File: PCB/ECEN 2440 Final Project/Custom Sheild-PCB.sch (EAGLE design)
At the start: 10 parts

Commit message: prettyfy schematic. vague shield board layout.
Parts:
- removed JP1: (no value), pinhead:PINHD-1X6
- added C1, C2, C3: 500n, rcl:C-USC0805
- added OI_1, OI_2, OI_3: (no value), pinhead:PINHD-1X3
- added R3, R4, R5: 100R, rcl:R-US_R0805
- added U$4: DRA_BREAKOUT, Custom Library:DRA_BREAKOUT
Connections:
- net CD1 renamed SD_CD1
- new net AUDIO_FILTERED: C3.1, R5.2, U$4.MIC_IN
- new net N$3: C1.1, R3.2, R4.1
- new net N$4: C2.1, R4.2, R5.1
- new net OI_1: OI_1.2, U$3.73
- new net OI_2: OI_2.2, U$3.70
- new net OI_3: OI_3.2, U$3.67
- new net PD_RADIO: U$4.PD
- new net RADIO_PD: U$3.35
- net +3V3: now also OI_1.3, OI_2.3, OI_3.3; no longer JP1.6
- net AUDIO_PTT: now also U$4.PTT; no longer JP1.4
- net AUDIO_PWM: now also R3.1; no longer JP1.3
- net GND: now also C1.2, C2.2, C3.2, OI_1.1, OI_2.1, OI_3.1, U$4.GND; no longer JP1.5
- net RX_RADIO: now also U$4.RX_RADIO; no longer JP1.2
- net TX_RADIO: now also U$4.TX_RADIO; no longer JP1.1
- net VCC: now also U$4.VBATT
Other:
- note added: "Altimeter and i2c"
- note added: "SD card options"
- note removed: "Radio Breakout Board Pin Hook Up"
- moved on the sheet: BATTERY, R1, R2, SD_BREAKOUT, SJ1, TEENSY, U$2

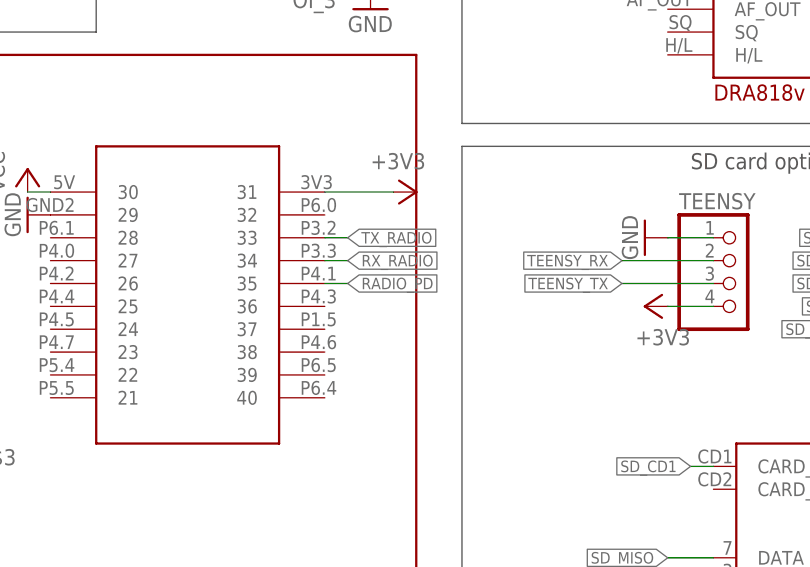
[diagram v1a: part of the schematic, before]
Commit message: changes to the traces of the shield board
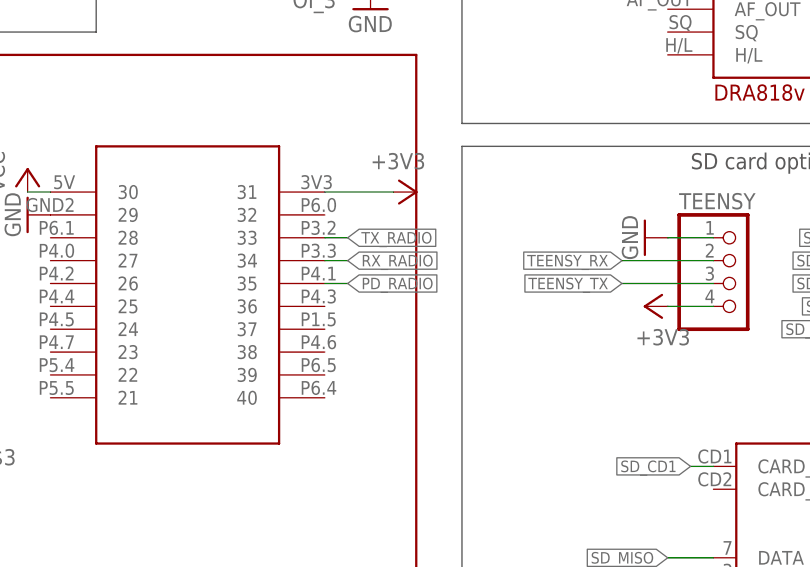
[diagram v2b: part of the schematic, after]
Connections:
- removed net RADIO_PD: U$3.35
- net PD_RADIO: now also U$3.35
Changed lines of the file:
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@@
 <?xml version="1.0" encoding="utf-8"?>
 <!DOCTYPE eagle SYSTEM "eagle.dtd">
-<eagle version="9.5.1">
+<eagle version="9.2.2">
 <drawing>
 <settings>
@@
 <label x="116.84" y="73.66" size="1.27" layer="95" rot="R180" xref="yes"/>
 </segment>
-</net>
-<net name="RADIO_PD" class="0">
 <segment>
 <pinref part="U$3" gate="MSP432" pin="35"/>

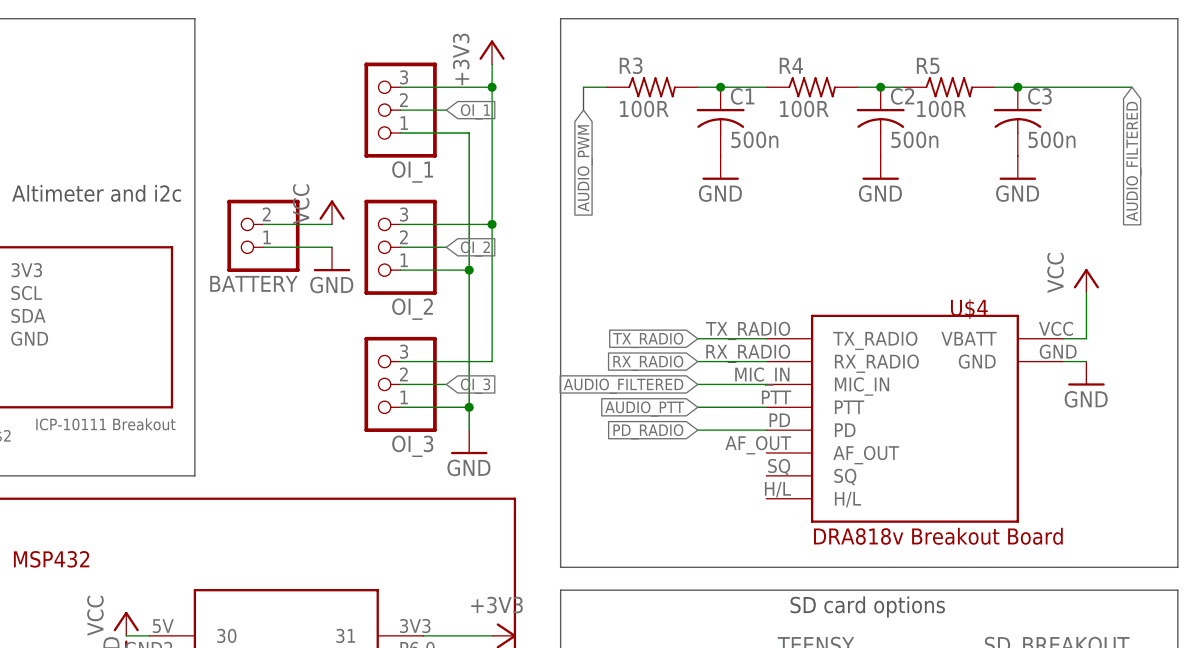
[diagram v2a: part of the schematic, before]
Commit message: changes to the traces of the sheild board
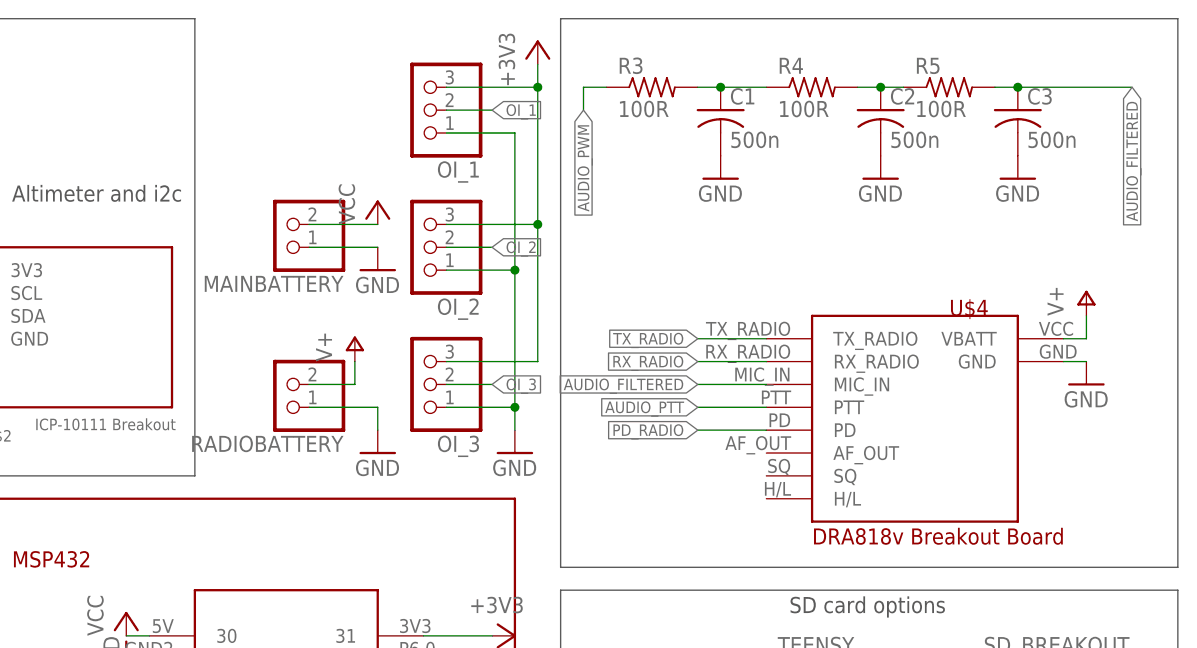
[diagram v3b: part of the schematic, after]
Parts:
- removed BATTERY: (no value), pinhead:PINHD-1X2
- added MAINBATTERY, RADIOBATTERY: (no value), pinhead:PINHD-1X2
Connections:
- new net V+: RADIOBATTERY.2, U$4.VBATT
- net GND: now also MAINBATTERY.1, RADIOBATTERY.1; no longer BATTERY.1
- net VCC: now also MAINBATTERY.2; no longer BATTERY.2, U$4.VBATT
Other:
- moved on the sheet: OI_1, OI_2, OI_3

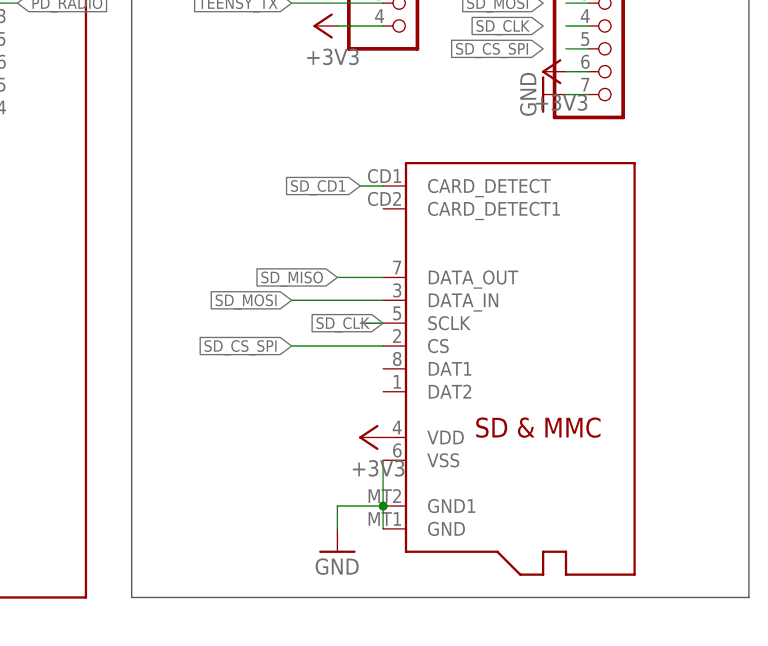
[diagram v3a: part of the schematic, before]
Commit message: changes to traces on sheild board
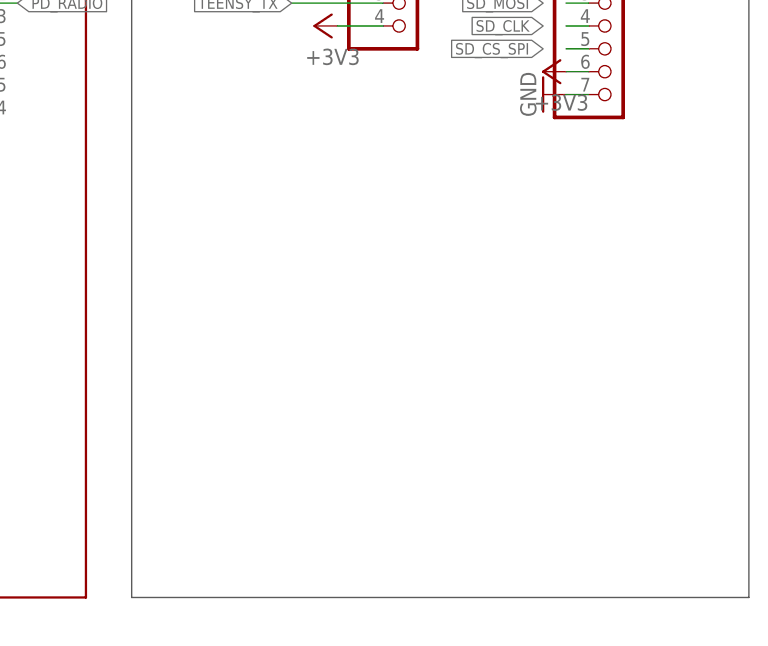
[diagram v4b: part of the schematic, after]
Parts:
- removed U$1: MICROSD, adafruit:MICROSD
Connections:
- net +3V3: no longer U$1.VDD
- net GND: no longer U$1.GND, U$1.GND1, U$1.VSS
- net SD_CD1: no longer U$1.CARD_DETECT
- net SD_CLK: no longer U$1.SCLK
- net SD_CS_SPI: no longer U$1.CS
- net SD_MISO: no longer U$1.DATA_OUT
- net SD_MOSI: no longer U$1.DATA_IN
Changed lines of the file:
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@@
 </classes>
 <parts>
-<part name="U$1" library="adafruit" library_urn="urn:adsk.eagle:library:420" deviceset="MICROSD" device="" package3d_urn="urn:adsk.eagle:package:6240723/1"/>
 <part name="U$2" library="Custom Library" deviceset="ALTIMETER" device=""/>
 <part name="U$3" library="Custom Library" deviceset="MSP432" device=""/>
 <part name="GND1" library="supply1" library_urn="urn:adsk.eagle:library:371" deviceset="GND" device=""/>
-<part name="GND2" library="supply1" library_urn="urn:adsk.eagle:library:371" deviceset="GND" device=""/>
 <part name="GND4" library="supply1" library_urn="urn:adsk.eagle:library:371" deviceset="GND" device=""/>
 <part name="GND5" library="supply1" library_urn="urn:adsk.eagle:library:371" deviceset="GND" device=""/>
 <part name="+3V1" library="supply1" library_urn="urn:adsk.eagle:library:371" deviceset="+3V3" device=""/>
 <part name="+3V2" library="supply1" library_urn="urn:adsk.eagle:library:371" deviceset="+3V3" device=""/>
-<part name="+3V3" library="supply1" library_urn="urn:adsk.eagle:library:371" deviceset="+3V3" device=""/>
 <part name="+3V5" library="supply1" library_urn="urn:adsk.eagle:library:371" deviceset="+3V3" device=""/>
 <part name="GND9" library="supply1" library_urn="urn:adsk.eagle:library:371" deviceset="GND" device=""/>
@@
 </plain>
 <instances>
-<instance part="U$1" gate="G$1" x="147.32" y="2.54" smashed="yes"/>
 <instance part="U$2" gate="G$1" x="38.1" y="76.2" smashed="yes">
 <attribute name="NAME" x="40.64" y="73.66" size="1.27" layer="95" rot="R180"/>
@@
 <attribute name="VALUE" x="25.4" y="76.2" size="1.778" layer="96"/>
 </instance>
-<instance part="GND2" gate="1" x="124.46" y="-20.32" smashed="yes">
-<attribute name="VALUE" x="121.92" y="-22.86" size="1.778" layer="96"/>
-</instance>
 <instance part="GND4" gate="1" x="25.4" y="-17.78" smashed="yes">
 <attribute name="VALUE" x="22.86" y="-20.32" size="1.778" layer="96"/>
@@
 <instance part="+3V2" gate="G$1" x="27.94" y="93.98" smashed="yes">
 <attribute name="VALUE" x="25.4" y="88.9" size="1.778" layer="96" rot="R90"/>
-</instance>
-<instance part="+3V3" gate="G$1" x="127" y="-7.62" smashed="yes" rot="R90">
-<attribute name="VALUE" x="132.08" y="-10.16" size="1.778" layer="96" rot="R180"/>
 </instance>
 <instance part="+3V5" gate="G$1" x="121.92" y="38.1" smashed="yes" rot="R90">
@@
 <net name="SD_CS_SPI" class="0">
 <segment>
-<pinref part="U$1" gate="G$1" pin="CS"/>
-<label x="119.38" y="2.54" size="1.27" layer="95" rot="R180" xref="yes"/>
-<wire x1="119.38" y1="2.54" x2="129.54" y2="2.54" width="0.1524" layer="91"/>
-</segment>
-<segment>
 <pinref part="U$3" gate="MSP432" pin="52"/>
 <wire x1="38.1" y1="-2.54" x2="38.1" y2="2.54" width="0.1524" layer="91"/>
@@
 <net name="SD_CLK" class="0">
 <segment>
-<pinref part="U$1" gate="G$1" pin="SCLK"/>
-<wire x1="129.54" y1="5.08" x2="127" y2="5.08" width="0.1524" layer="91"/>
-<label x="129.54" y="5.08" size="1.27" layer="95" rot="R180" xref="yes"/>
-</segment>
-<segment>
 <pinref part="U$3" gate="MSP432" pin="51"/>
 <wire x1="38.1" y1="-10.16" x2="38.1" y2="-15.24" width="0.1524" layer="91"/>
@@
 <net name="SD_MISO" class="0">
 <segment>
-<pinref part="U$1" gate="G$1" pin="DATA_OUT"/>
-<wire x1="129.54" y1="10.16" x2="124.46" y2="10.16" width="0.1524" layer="91"/>
-<label x="124.46" y="10.16" size="1.27" layer="95" rot="R180" xref="yes"/>
-</segment>
-<segment>
 <pinref part="U$3" gate="MSP432" pin="50"/>
 <wire x1="35.56" y1="-2.54" x2="35.56" y2="2.54" width="0.1524" layer="91"/>
@@
 </net>
 <net name="SD_MOSI" class="0">
-<segment>
-<pinref part="U$1" gate="G$1" pin="DATA_IN"/>
-<wire x1="129.54" y1="7.62" x2="119.38" y2="7.62" width="0.1524" layer="91"/>
-<label x="119.38" y="7.62" size="1.27" layer="95" rot="R180" xref="yes"/>
-</segment>
 <segment>
 <pinref part="U$3" gate="MSP432" pin="49"/>
@@
 <wire x1="27.94" y1="83.82" x2="33.02" y2="83.82" width="0.1524" layer="91"/>
 <pinref part="GND1" gate="1" pin="GND"/>
-</segment>
-<segment>
-<pinref part="U$1" gate="G$1" pin="GND"/>
-<pinref part="U$1" gate="G$1" pin="GND1"/>
-<wire x1="129.54" y1="-15.24" x2="129.54" y2="-17.78" width="0.1524" layer="91"/>
-<pinref part="GND2" gate="1" pin="GND"/>
-<wire x1="124.46" y1="-17.78" x2="124.46" y2="-15.24" width="0.1524" layer="91"/>
-<wire x1="124.46" y1="-15.24" x2="129.54" y2="-15.24" width="0.1524" layer="91"/>
-<junction x="129.54" y="-15.24"/>
-<pinref part="U$1" gate="G$1" pin="VSS"/>
-<wire x1="129.54" y1="-10.16" x2="129.54" y2="-15.24" width="0.1524" layer="91"/>
 </segment>
 <segment>
@@
 </segment>
 <segment>
-<pinref part="U$1" gate="G$1" pin="VDD"/>
-<pinref part="+3V3" gate="G$1" pin="+3V3"/>
-</segment>
-<segment>
 <pinref part="+3V5" gate="G$1" pin="+3V3"/>
 <pinref part="TEENSY" gate="A" pin="4"/>
@@
 <net name="SD_CD1" class="0">
 <segment>
-<pinref part="U$1" gate="G$1" pin="CARD_DETECT"/>
-<wire x1="129.54" y1="20.32" x2="127" y2="20.32" width="0.1524" layer="91"/>
-<label x="127" y="20.32" size="1.27" layer="95" rot="R180" xref="yes"/>
-</segment>
-<segment>
 <pinref part="U$3" gate="MSP432" pin="48"/>

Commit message: final board maybe??
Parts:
- removed RADIOBATTERY: (no value), pinhead:PINHD-1X2
- added C4, C5: (no value), rcl:CPOL-USA
- added U$1: BDXXC0A-CBD33C0AWFP-CE2, Custom Library:BDXXC0A-CBD33C0AWFP-CE2
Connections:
- removed net V+: RADIOBATTERY.2, U$4.VBATT
- net +3V3: now also C5.+, U$1.VO
- net GND: now also C4.-, C5.-, U$1.GND; no longer RADIOBATTERY.1
- net VCC: now also C4.+, U$1.CTL, U$1.VCC, U$4.VBATT; no longer U$3.30, U$3.45, U$3.46
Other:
- moved on the sheet: C1, C2, C3, MAINBATTERY, OI_1, OI_2, OI_3, R1, R2, R3, R4, R5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

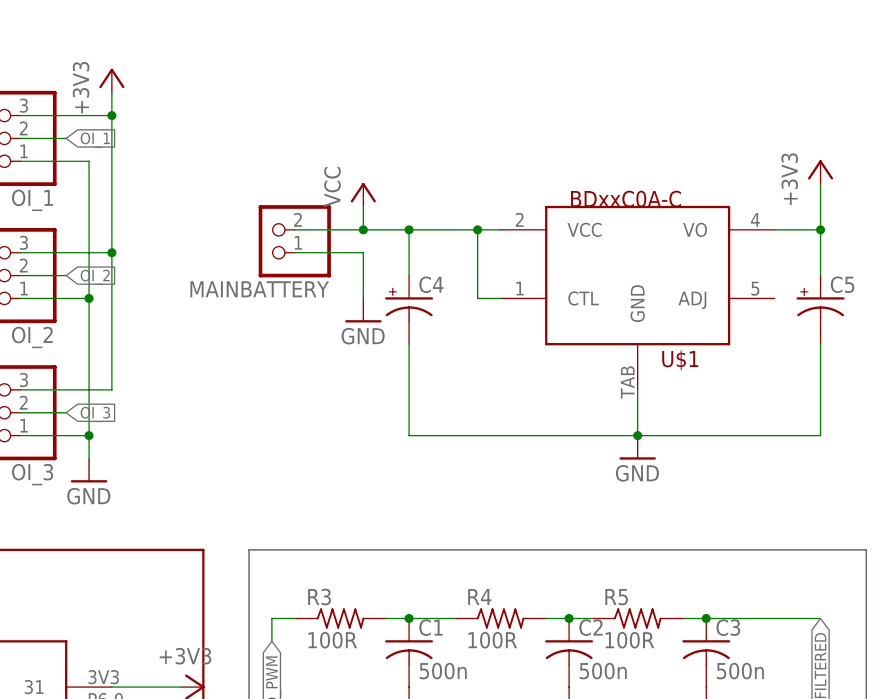
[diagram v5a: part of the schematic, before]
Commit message: add voltage test points
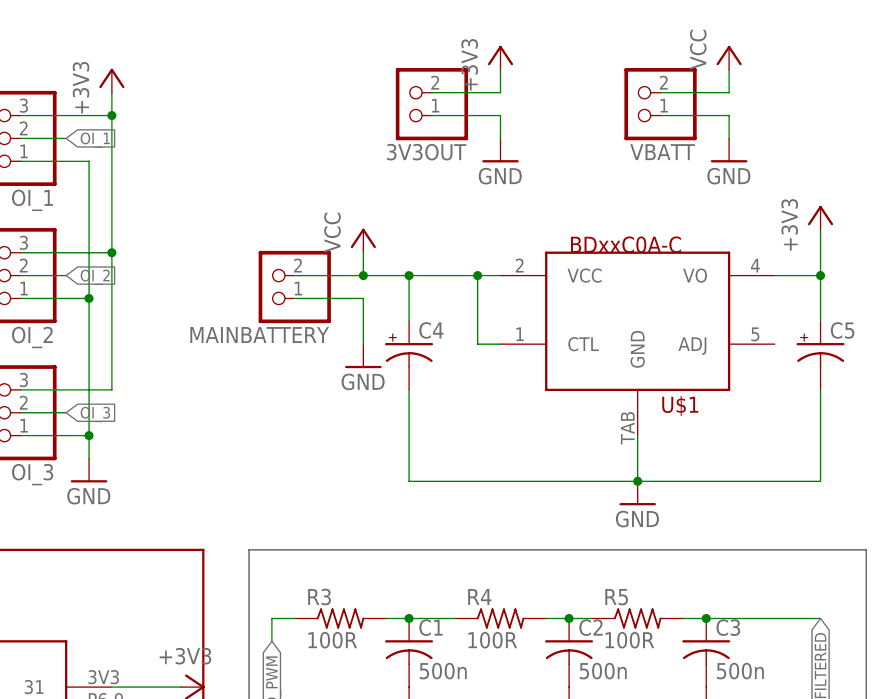
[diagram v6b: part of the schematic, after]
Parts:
- added 3V3OUT, VBATT: (no value), pinhead:PINHD-1X2
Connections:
- net +3V3: now also 3V3OUT.2
- net GND: now also 3V3OUT.1, VBATT.1
- net VCC: now also VBATT.2
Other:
- moved on the sheet: C4, C5, MAINBATTERY, U$1

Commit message: Fix MSP432 footprint
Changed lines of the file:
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@@
 <segment>
 <pinref part="SD_BREAKOUT" gate="A" pin="5"/>
-<wire x1="152.4" y1="-15.24" x2="149.86" y2="-15.24" width="0.1524" layer="91"/>
+<wire x1="152.4" y1="-15.24" x2="147.32" y2="-15.24" width="0.1524" layer="91"/>
 <label x="147.32" y="-15.24" size="1.27" layer="95" rot="R180" xref="yes"/>
 </segment>
@@
 <segment>
 <pinref part="SD_BREAKOUT" gate="A" pin="4"/>
-<wire x1="152.4" y1="-12.7" x2="149.86" y2="-12.7" width="0.1524" layer="91"/>
+<wire x1="152.4" y1="-12.7" x2="147.32" y2="-12.7" width="0.1524" layer="91"/>
 <label x="147.32" y="-12.7" size="1.27" layer="95" rot="R180" xref="yes"/>
 </segment>
@@
 <segment>
 <pinref part="SD_BREAKOUT" gate="A" pin="2"/>
-<wire x1="152.4" y1="-7.62" x2="149.86" y2="-7.62" width="0.1524" layer="91"/>
+<wire x1="152.4" y1="-7.62" x2="147.32" y2="-7.62" width="0.1524" layer="91"/>
 <label x="147.32" y="-7.62" size="1.27" layer="95" rot="R180" xref="yes"/>
 </segment>
@@
 <segment>
 <pinref part="SD_BREAKOUT" gate="A" pin="3"/>
-<wire x1="152.4" y1="-10.16" x2="149.86" y2="-10.16" width="0.1524" layer="91"/>
+<wire x1="152.4" y1="-10.16" x2="147.32" y2="-10.16" width="0.1524" layer="91"/>
 <label x="147.32" y="-10.16" size="1.27" layer="95" rot="R180" xref="yes"/>
 </segment>
@@
 <segment>
 <pinref part="SD_BREAKOUT" gate="A" pin="1"/>
-<wire x1="152.4" y1="-5.08" x2="149.86" y2="-5.08" width="0.1524" layer="91"/>
+<wire x1="152.4" y1="-5.08" x2="147.32" y2="-5.08" width="0.1524" layer="91"/>
 <label x="147.32" y="-5.08" size="1.27" layer="95" rot="R180" xref="yes"/>
 </segment>

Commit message: really important commit
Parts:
- added U$5: MEOWTH, Custom Library:MEOWTH
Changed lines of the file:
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@@
 <part name="+3V8" library="supply1" library_urn="urn:adsk.eagle:library:371" deviceset="+3V3" device=""/>
 <part name="GND12" library="supply1" library_urn="urn:adsk.eagle:library:371" deviceset="GND" device=""/>
+<part name="U$5" library="Custom Library" deviceset="MEOWTH" device=""/>
 </parts>
 <sheets>
@@
 <attribute name="VALUE" x="127" y="106.68" size="1.778" layer="96"/>
 </instance>
+<instance part="U$5" gate="G$1" x="104.14" y="68.58" smashed="yes"/>
 </instances>
 <busses>
